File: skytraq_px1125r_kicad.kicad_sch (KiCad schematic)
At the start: 11 parts, among them J1 Conn_01x04, J2 SMA, J3 SH_Conn_01x04, J4 Conn_01x04, U1 Skytraq_PX1125R

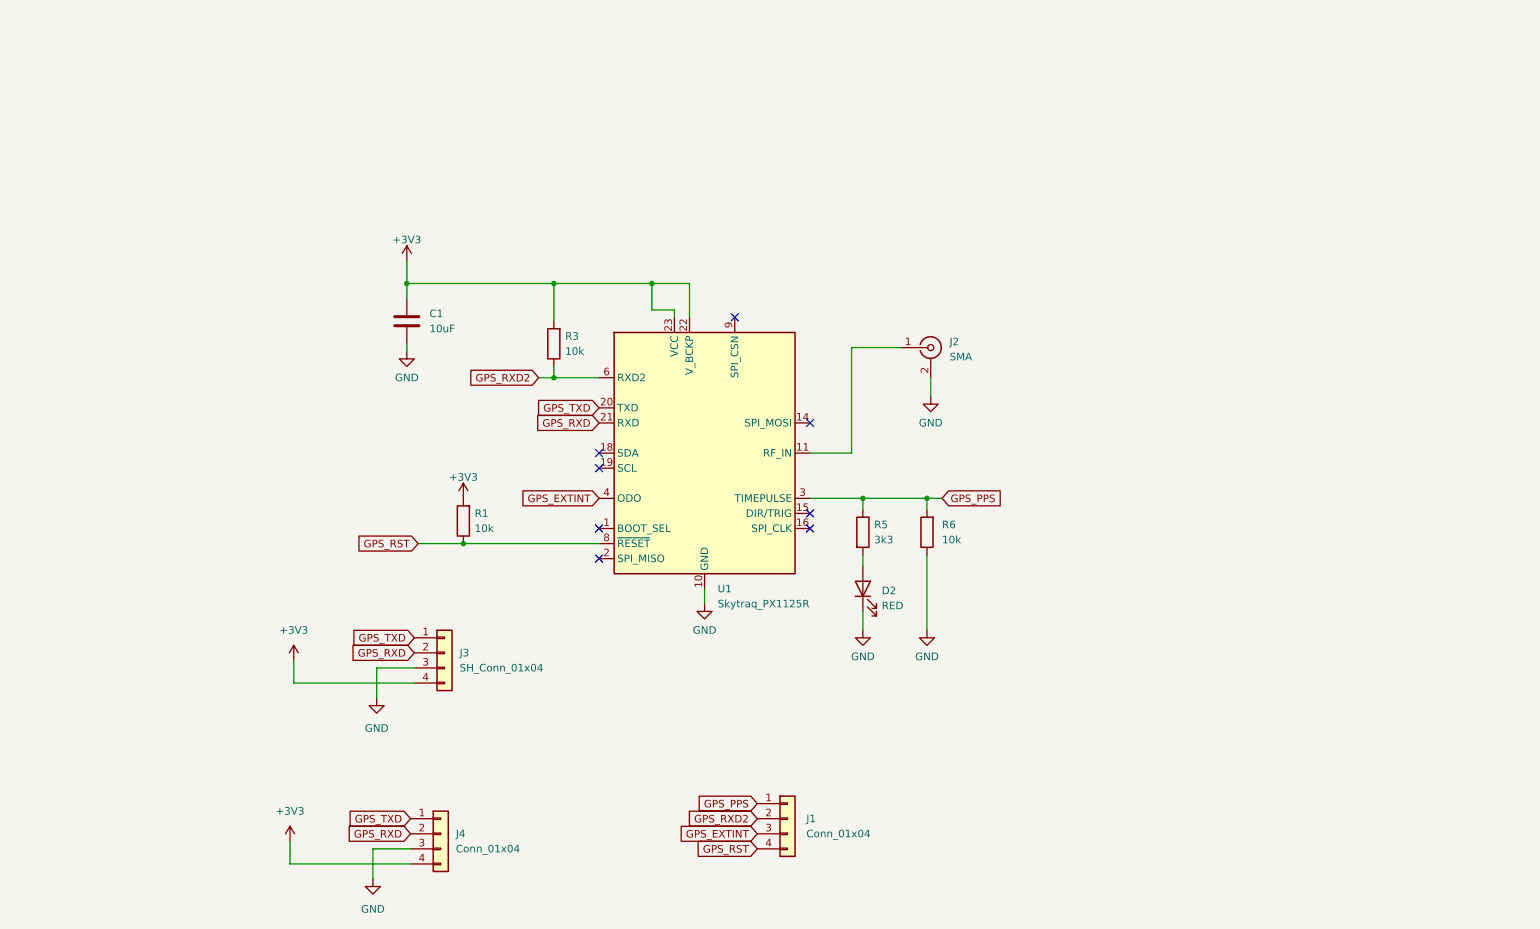
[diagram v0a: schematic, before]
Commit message: 36x36 flight controller board
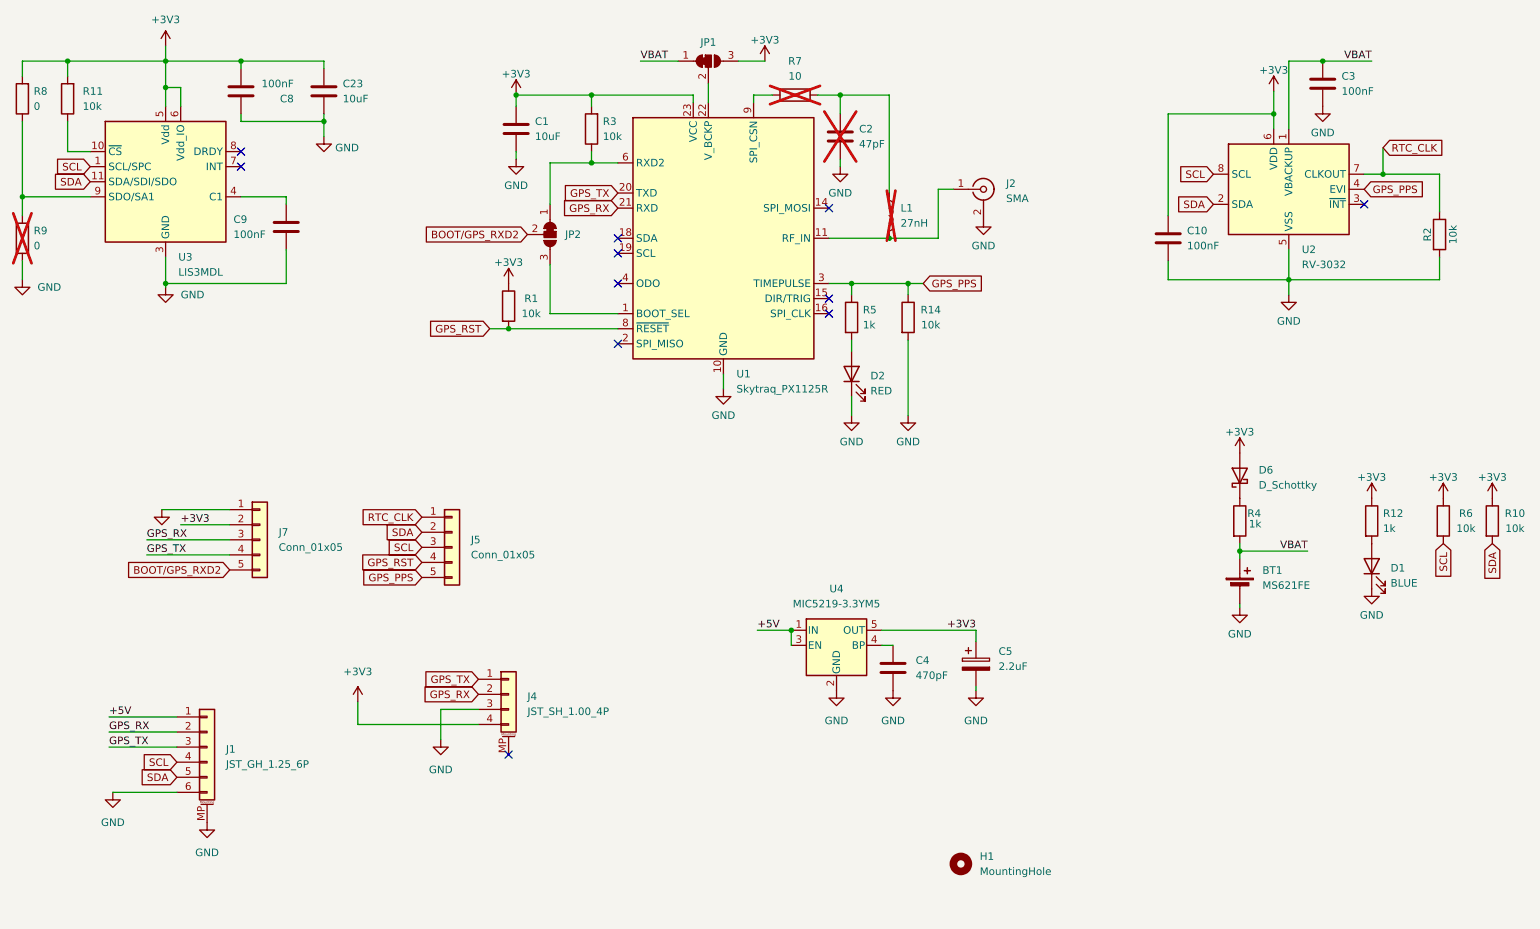
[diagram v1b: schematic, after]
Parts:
- removed J1, J4: Conn_01x04, Connector_PinHeader_2.54mm:PinHeader_1x04_P2.54mm_Vertical, symbol Connector_Generic:Conn_01x04
- removed J3: SH_Conn_01x04, Connector_JST:JST_SH_SM04B-SRSS-TB_1x04-1MP_P1.00mm_Horizontal, symbol Connector_Generic:Conn_01x04
- added BT1: MS621FE, Battery:BatteryHolder_Seiko_MS621F, symbol Device:Battery_Cell
- added C10, C3, C8, C9: 100nF, Capacitor_SMD:C_0402_1005Metric, symbol Device:C
- added C2: 47pF, Capacitor_SMD:C_0603_1608Metric, symbol Device:C
- added C23: 10uF, Capacitor_SMD:C_0603_1608Metric, symbol Device:C
- added C4: 470pF, Capacitor_SMD:C_0603_1608Metric_Pad1.08x0.95mm_HandSolder, symbol Device:C
- added C5: 2.2uF, Capacitor_Tantalum_SMD:CP_EIA-3216-18_Kemet-A, symbol Device:C_Polarized
- added D1: BLUE, LED_SMD:LED_0603_1608Metric, symbol Device:LED
- added D6: D_Schottky, Diode_SMD:D_SMB, symbol Device:D_Schottky
- added H1: MountingHole, MountingHole:MountingHole_3.2mm_M3, symbol Mechanical:MountingHole
- added J1: JST_GH_1.25_6P, Connector_JST:JST_GH_SM06B-GHS-TB_1x06-1MP_P1.25mm_Horizontal, symbol Connector_Generic_MountingPin:Conn_01x06_MountingPin
- added J4: JST_SH_1.00_4P, Connector_JST:JST_SH_SM04B-SRSS-TB_1x04-1MP_P1.00mm_Horizontal, symbol Connector_Generic_MountingPin:Conn_01x04_MountingPin
- added J5, J7: Conn_01x05, Connector_PinHeader_2.54mm:PinHeader_1x05_P2.54mm_Horizontal, symbol Connector_Generic:Conn_01x05
- added JP1, JP2: SolderJumper_3_Bridged12, Jumper:SolderJumper-3_P1.3mm_Bridged12_RoundedPad1.0x1.5mm, symbol Jumper:SolderJumper_3_Bridged12
- added L1: 27nH, Inductor_SMD:L_0603_1608Metric, symbol Device:L
- added R10, R11, R14, R2: 10k, Resistor_SMD:R_0603_1608Metric, symbol Device:R
- added R12, R4: 1k, Resistor_SMD:R_0603_1608Metric, symbol Device:R
- added R7: 10, Resistor_SMD:R_0603_1608Metric, symbol Device:R
- added R8, R9: 0, Resistor_SMD:R_0603_1608Metric, symbol Device:R
- added U2: RV-3032, MyFootprints:RV-3032, symbol MySymbols:RV-3032
- added U3: LIS3MDL, footprint_JLCPCB:LGA-12_L2.0-W2.0-P0.50-BL, symbol Sensor_Magnetic:LIS3MDL
- added U4: MIC5219-3.3YM5, Package_TO_SOT_SMD:SOT-23-5, symbol Regulator_Linear:MIC5219-3.3YM5
- C1: footprint Capacitor_SMD:C_0805_2012Metric_Pad1.18x1.45mm_HandSolder -> Capacitor_SMD:C_0603_1608Metric; Note (none) -> Low ESR! X7R; OriginalVal 4u7/10V -> (none)
- D2: footprint LED_SMD:LED_0805_2012Metric_Pad1.15x1.40mm_HandSolder -> LED_SMD:LED_0603_1608Metric; LCSC (none) -> C2286; Note (none) -> PPS
- J2: footprint Connector_Coaxial:SMA_Amphenol_901-143_Horizontal -> footprint_JLCPCB:SMA-SMD_BWSMA-KE-P001; LCSC (none) -> C496550
- R1, R3, R6: footprint Resistor_SMD:R_0805_2012Metric_Pad1.20x1.40mm_HandSolder -> Resistor_SMD:R_0603_1608Metric; LCSC (none) -> C25804
- R5: value 3k3 -> 1k; footprint Resistor_SMD:R_0805_2012Metric_Pad1.20x1.40mm_HandSolder -> Resistor_SMD:R_0603_1608Metric; LCSC (none) -> C21190; OriginalVal 4k7 -> (none)
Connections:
- net +3V3: now also C1.1, R1.1, R6.1, C10.1, C23.2, C5.1, C8.1, D6.2 (A), J4.4 (Pin_4), J7.2 (Pin_2), JP1.3 (B), R10.1, R11.2, R12.1, R8.2, U2.6 (VDD), U3.5 (Vdd), U3.6 (Vdd_IO), U4.5 (OUT); no longer C1.2, R1.2, U1.22 (V_BCKP)
- net GND: now also C1.2, BT1.2 (-), C10.2, C2.2, C23.1, C3.2, C4.2, C5.2, C8.2, C9.1, D1.1 (K), J1.6 (Pin_6), J1.MP (MountPin), J4.3 (Pin_3), J7.1 (Pin_1), R14.2, R2.2, R9.1, U2.5 (VSS), U3.12 (GND), U3.2 (GND), U3.3 (GND), U4.2 (GND); no longer C1.1, R6.1
- net GPS_PPS: now also J5.5 (Pin_5), R14.1, U2.4 (EVI); no longer R6.2
- net GPS_RST: now also R1.2, J5.4 (Pin_4); no longer R1.1
- net at J2.1 (In), U1.11 (RF_IN): now also L1.2
- net at U1.1 (BOOT_SEL): now also JP2.3 (B)
- net at U1.9 (SPI_CSN): now also R7.1
- net GPS_EXTINT: no longer names the net of U1.4 (ODO)
- net GPS_RXD renamed GPS_RX
- net GPS_RX: now also J1.2 (Pin_2), J4.2 (Pin_2), J7.3 (Pin_3)
- net GPS_RXD2: no longer names the net of R3.1, U1.6 (RXD2)
- net GPS_RXD2: now also JP2.1 (A)
- net GPS_TXD renamed GPS_TX
- net GPS_TX: now also J1.3 (Pin_3), J4.1 (Pin_1), J7.4 (Pin_4)
- new net: C2.1, L1.1, R7.2
- new net: R8.1, R9.2, U3.9 (SDO/SA1)
- new net: C4.1, U4.4 (BP)
- new net: D1.2 (A), R12.2
- new net: JP1.2 (C), U1.22 (V_BCKP)
- new net: C9.2, U3.4 (C1)
- new net: D6.1 (K), R4.1
- new net: R11.1, U3.10 (~{CS})
- new net +5V: J1.1 (Pin_1), U4.1 (IN), U4.3 (EN)
- new net BOOT/GPS_RXD2: J7.5 (Pin_5), JP2.2 (C)
- new net RTC_CLK: J5.1 (Pin_1), R2.1, U2.7 (CLKOUT)
- new net SCL: J1.4 (Pin_4), J5.3 (Pin_3), R6.2, U2.8 (SCL), U3.1 (SCL/SPC)
- new net SDA: J1.5 (Pin_5), J5.2 (Pin_2), R10.2, U2.2 (SDA), U3.11 (SDA/SDI/SDO)
- new net VBAT: BT1.1 (+), C3.1, JP1.1 (A), R4.2, U2.1 (VBACKUP)
- no-connect marks 8 -> 11
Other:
- moved on the sheet: J2, R3, U1

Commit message: with px1105 unfinished
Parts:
- removed C4: 470pF, Capacitor_SMD:C_0603_1608Metric_Pad1.08x0.95mm_HandSolder, symbol Device:C
- removed C5: 2.2uF, Capacitor_Tantalum_SMD:CP_EIA-3216-18_Kemet-A, symbol Device:C_Polarized
- removed J4: JST_SH_1.00_4P, Connector_JST:JST_SH_SM04B-SRSS-TB_1x04-1MP_P1.00mm_Horizontal, symbol Connector_Generic_MountingPin:Conn_01x04_MountingPin
- removed J5, J7: Conn_01x05, Connector_PinHeader_2.54mm:PinHeader_1x05_P2.54mm_Horizontal, symbol Connector_Generic:Conn_01x05
- removed U4: MIC5219-3.3YM5, Package_TO_SOT_SMD:SOT-23-5, symbol Regulator_Linear:MIC5219-3.3YM5
- added C6: 22uF, Capacitor_Tantalum_SMD:CP_EIA-3216-18_Kemet-A, symbol Device:C_Polarized
- added C7: 10uF, Capacitor_SMD:C_0603_1608Metric, symbol Device:C
- added J5: Conn_01x04, Connector_PinSocket_2.54mm:PinSocket_1x04_P2.54mm_Vertical, symbol Connector_Generic:Conn_01x04
- added J7: Conn_01x06, Connector_PinHeader_2.54mm:PinHeader_1x06_P2.54mm_Vertical, symbol Connector_Generic:Conn_01x06
- added U5: ~, MyFootprints:skytraq_px1105, symbol MySkyTraqSymbols:SkyTraq_PX1105
- added U6: AMS1117-3.3, Package_TO_SOT_SMD:SOT-223-3_TabPin2, symbol Regulator_Linear:AMS1117-3.3
- D6: footprint Diode_SMD:D_SMB -> Diode_SMD:D_SOD-323
- J2: footprint footprint_JLCPCB:SMA-SMD_BWSMA-KE-P001 -> footprint_JLCPCB:SMA-SMD_BWSMA-KE-P001_Symmetric
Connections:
- net +3V3: now also C6.1, J7.2 (Pin_2), U5.8 (VCC), U6.2 (VO)
- net +5V: now also C7.2, U6.3 (VI)
- net BOOT/GPS_RXD2: now also J7.6 (Pin_6)
- net GND: now also C6.2, C7.1, J7.1 (Pin_1), U5.1 (GND), U6.1 (GND)
- net GPS_PPS: now also J7.5 (Pin_5), U5.4 (PPS)
- net GPS_RST: now also J5.4 (Pin_4), U5.9 (~{RESET})
- net GPS_RX: now also J7.3 (Pin_3), U5.3 (RXD)
- net GPS_TX: now also J7.4 (Pin_4), U5.2 (TXD)
- net RTC_CLK: now also J5.1 (Pin_1)
- net SCL: now also J5.3 (Pin_3)
- net SDA: now also J5.2 (Pin_2)
- net GPS_RF: now reaches J2.1 (In), L1.2, U1.11 (RF_IN)
- net GPS_RF: now also U5.11 (RF_IN)
- net GPS_V_BCKP: now reaches JP1.2 (C), U1.22 (V_BCKP)
- net GPS_V_BCKP: now also U5.6 (V_BCKP)
- net GPS_RX2: now reaches JP2.1 (A), R3.1, U1.6 (RXD2)
- net GPS_RX2: now also U5.15 (RXD2)
- net GPS_BOOT: now reaches JP2.3 (B), U1.1 (BOOT_SEL)
- net GPS_BOOT: now also U5.18 (BOOT_SEL)
- no-connect marks 11 -> 14
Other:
- moved on the sheet: BT1, C1, D1, D6, J1, JP1, JP2, R1, R10, R12, R3, R4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

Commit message: px1105 4-layers boar
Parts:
- removed J5: Conn_01x04, Connector_PinSocket_2.54mm:PinSocket_1x04_P2.54mm_Vertical, symbol Connector_Generic:Conn_01x04
- added C4: 100nF, Capacitor_SMD:C_0402_1005Metric, symbol Device:C
- added C5: 10uF, Capacitor_SMD:C_0603_1608Metric, symbol Device:C
- added J3: JST_GH_1.25_6P, Connector_JST:JST_GH_SM06B-GHS-TB_1x06-1MP_P1.25mm_Horizontal, symbol Connector_Generic_MountingPin:Conn_01x06_MountingPin
- added J5: Conn_01x06, Connector_PinHeader_2.54mm:PinHeader_1x06_P2.54mm_Vertical, symbol Connector_Generic:Conn_01x06
- U6: footprint Package_TO_SOT_SMD:SOT-223-3_TabPin2 -> Package_TO_SOT_SMD:SOT-89-3
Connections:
- net +3V3: now also J7.1 (Pin_1), C5.1; no longer J7.2 (Pin_2)
- net +5V: now also J3.1 (Pin_1), J5.1 (Pin_1)
- net BOOT/GPS_RXD2: now also J3.2 (Pin_2)
- net GND: now also J7.2 (Pin_2), C4.2, C5.2, J3.6 (Pin_6), J5.2 (Pin_2); no longer J1.MP (MountPin), J7.1 (Pin_1)
- net GPS_PPS: now also J3.3 (Pin_3)
- net GPS_RST: now also J3.5 (Pin_5), J5.6 (Pin_6)
- net GPS_V_BCKP: now also C4.1
- net RTC_CLK: now also J3.4 (Pin_4), J5.3 (Pin_3)
- net SCL: now also J5.5 (Pin_5)
- net SDA: now also J5.4 (Pin_4)
- no-connect marks 14 -> 16
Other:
- moved on the sheet: U5

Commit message: added 2 M3 mounting holes
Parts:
- added D3: GREEN, LED_SMD:LED_0603_1608Metric, symbol Device:LED
- added H2, H3, H4: MountingHole, MountingHole:MountingHole_3.2mm_M3, symbol Mechanical:MountingHole
- added R13: 1k, Resistor_SMD:R_0603_1608Metric, symbol Device:R
- C4: footprint Capacitor_SMD:C_0402_1005Metric -> Capacitor_SMD:C_0805_2012Metric_Pad1.18x1.45mm_HandSolder; LCSC C1525 -> (none); Note Low ESR! X7R -> (none); now left out of the parts list
- C5: footprint Capacitor_SMD:C_0603_1608Metric -> Capacitor_SMD:C_0805_2012Metric_Pad1.18x1.45mm_HandSolder; LCSC C19702 -> (none); Note Low ESR! X7R -> (none); now left out of the parts list
- J2: footprint footprint_JLCPCB:SMA-SMD_BWSMA-KE-P001_Symmetric -> footprint:SMA-SMD_BWSMA-KE-P001_Symmetric
- U3: footprint footprint_JLCPCB:LGA-12_L2.0-W2.0-P0.50-BL -> footprint:LGA-12_L2.0-W2.0-P0.50-BL
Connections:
- net +3V3: now also R13.1
- net GPS_RX2: now also D3.1 (K)
- net BOOT/GPS_RXD2 renamed BOOT/GPS_RX2
- new net: D3.2 (A), R13.2

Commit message: one more M3 hole
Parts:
- C3: value 100nF -> 10uF; footprint Capacitor_SMD:C_0402_1005Metric -> Capacitor_SMD:C_0603_1608Metric; LCSC C1525 -> C19702
- U5: value ~ -> SkyTraq_PX1105; now left out of the parts list
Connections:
- net GPS_V_BCKP: now also C3.1
- net VBAT: no longer C3.1
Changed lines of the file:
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@@
 	)
 	(junction
-		(at 241.935 26.67)
-		(diameter 0)
-		(color 0 0 0 0)
-	)
-	(junction
 		(at 252.095 45.72)
 		(diameter 0)
@@
 	(wire
 		(pts
+			(xy 138.557 27.178) (xy 138.557 27.305)
+		)
+		(stroke
+			(width 0)
+			(type default)
+		)
+	)
+	(wire
+		(pts
 			(xy 111.125 43.815) (xy 123.19 43.815)
 		)
@@
 	(wire
 		(pts
-			(xy 236.22 26.67) (xy 236.22 38.1)
+			(xy 236.22 35.306) (xy 236.22 38.1)
 		)
 		(stroke
@@
 	(wire
 		(pts
+			(xy 138.557 27.305) (xy 138.43 27.305)
+		)
+		(stroke
+			(width 0)
+			(type default)
+		)
+	)
+	(wire
+		(pts
 			(xy 30.48 36.83) (xy 30.48 41.91)
 		)
@@
 	(wire
 		(pts
-			(xy 236.22 26.67) (xy 241.935 26.67)
+			(xy 236.22 35.306) (xy 240.284 35.306)
 		)
 		(stroke
@@
 	(wire
 		(pts
-			(xy 241.935 26.67) (xy 250.19 26.67)
-		)
-		(stroke
-			(width 0)
-			(type default)
-		)
-	)
-	(wire
-		(pts
 			(xy 67.31 64.135) (xy 46.99 64.135)
 		)
@@
 	(wire
 		(pts
-			(xy 150.495 27.305) (xy 138.43 27.305)
+			(xy 150.622 27.178) (xy 138.557 27.178)
 		)
 		(stroke
@@
 	)
 	(label "VBAT"
-		(at 250.19 26.67 180)
+		(at 240.284 35.306 180)
 		(effects
 			(font
@@
 	)
 	(label "GPS_V_BCKP"
-		(at 150.495 27.305 180)
+		(at 150.622 27.178 180)
 		(effects
 			(font
@@
 		(on_board yes)
 		(dnp yes)
-		(fields_autoplaced yes)
 		(property "Reference" "R7"
-			(at 153.035 26.67 90)
+			(at 147.828 31.242 90)
 			(effects
 				(font
@@
 		)
 		(property "Value" "10"
-			(at 153.035 29.21 90)
+			(at 152.908 32.512 90)
 			(effects
 				(font
@@
 	(symbol
 		(lib_id "power:GND")
-		(at 241.935 34.29 0)
-		(unit 1)
-		(exclude_from_sim no)
-		(in_bom yes)
-		(on_board yes)
-		(dnp no)
-		(fields_autoplaced yes)
-		(property "Reference" "#PWR04"
-			(at 241.935 40.64 0)
-			(effects
-				(font
-					(size 1.27 1.27)
-				)
-				(hide yes)
-			)
-		)
-		(property "Value" "GND"
-			(at 241.935 38.735 0)
-			(effects
-				(font
-					(size 1.27 1.27)
-				)
-			)
-		)
-		(property "Footprint" ""
-			(at 241.935 34.29 0)
-			(effects
-				(font
-					(size 1.27 1.27)
-				)
-				(hide yes)
-			)
-		)
-		(property "Datasheet" "~"
-			(at 241.935 34.29 0)
-			(effects
-				(font
-					(size 1.27 1.27)
-				)
-				(hide yes)
-			)
-		)
-		(property "Description" "Power symbol creates a global label with name \"GND\" , ground"
-			(at 241.935 34.29 0)
-			(effects
-				(font
-					(size 1.27 1.27)
-				)
-				(hide yes)
-			)
-		)
-		(pin "1"
-		)
-		(instances
-			(project "skytraq_px1125r_kicad"
-				(path "/f8f1d4cf-0f7a-4055-9a9d-a328f34ee721"
-					(reference "#PWR04")
-					(unit 1)
-				)
-			)
-		)
-	)
-	(symbol
-		(lib_id "power:GND")
 		(at 123.825 109.22 0)
 		(unit 1)
@@
 		(unit 1)
 		(exclude_from_sim no)
-		(in_bom yes)
+		(in_bom no)
 		(on_board yes)
 		(dnp no)
@@
 			)
 		)
-		(property "Value" "~"
+		(property "Value" "SkyTraq_PX1105"
 			(at 138.6683 142.24 0)
 			(effects
@@
 	)
 	(symbol
+		(lib_id "power:GND")
+		(at 158.242 27.178 0)
+		(unit 1)
+		(exclude_from_sim no)
+		(in_bom yes)
+		(on_board yes)
+		(dnp no)
+		(fields_autoplaced yes)
+		(property "Reference" "#PWR04"
+			(at 158.242 33.528 0)
+			(effects
+				(font
+					(size 1.27 1.27)
+				)
+				(hide yes)
+			)
+		)
+		(property "Value" "GND"
+			(at 158.242 31.623 0)
+			(effects
+				(font
+					(size 1.27 1.27)
+				)
+			)
+		)
+		(property "Footprint" ""
+			(at 158.242 27.178 0)
+			(effects
+				(font
+					(size 1.27 1.27)
+				)
+				(hide yes)
+			)
+		)
+		(property "Datasheet" ""
+			(at 158.242 27.178 0)
+			(effects
+				(font
+					(size 1.27 1.27)
+				)
+				(hide yes)
+			)
+		)
+		(property "Description" ""
+			(at 158.242 27.178 0)
+			(effects
+				(font
+					(size 1.27 1.27)
+				)
+			)
+		)
+		(pin "1"
+		)
+		(instances
+			(project "skytraq_px1125r_kicad"
+				(path "/f8f1d4cf-0f7a-4055-9a9d-a328f34ee721"
+					(reference "#PWR04")
+					(unit 1)
+				)
+			)
+		)
+	)
+	(symbol
 		(lib_id "Device:C")
 		(at 98.425 38.1 0)
@@
 	)
 	(symbol
-		(lib_id "Device:C")
-		(at 241.935 30.48 0)
-		(unit 1)
-		(exclude_from_sim no)
-		(in_bom yes)
-		(on_board yes)
-		(dnp no)
-		(property "Reference" "C3"
-			(at 245.11 29.21 0)
-			(effects
-				(font
-					(size 1.27 1.27)
-				)
-				(justify left)
-			)
-		)
-		(property "Value" "100nF"
-			(at 245.11 31.75 0)
-			(effects
-				(font
-					(size 1.27 1.27)
-				)
-				(justify left)
-			)
-		)
-		(property "Footprint" "Capacitor_SMD:C_0402_1005Metric"
-			(at 242.9002 34.29 0)
-			(effects
-				(font
-					(size 1.27 1.27)
-				)
-				(hide yes)
-			)
-		)
-		(property "Datasheet" "~"
-			(at 241.935 30.48 0)
-			(effects
-				(font
-					(size 1.27 1.27)
-				)
-				(hide yes)
-			)
-		)
-		(property "Description" "Unpolarized capacitor"
-			(at 241.935 30.48 0)
-			(effects
-				(font
-					(size 1.27 1.27)
-				)
-				(hide yes)
-			)
-		)
-		(property "LCSC" "C1525"
-			(at 241.935 30.48 0)
-			(effects
-				(font
-					(size 1.27 1.27)
-				)
-				(hide yes)
-			)
-		)
-		(property "Note" "Low ESR! X7R"
-			(at 241.935 30.48 0)
-			(effects
-				(font
-					(size 1.27 1.27)
-				)
-				(hide yes)
-			)
-		)
-		(pin "1"
-		)
-		(pin "2"
-		)
-		(instances
-			(project "skytraq_px1125r_kicad"
-				(path "/f8f1d4cf-0f7a-4055-9a9d-a328f34ee721"
-					(reference "C3")
-					(unit 1)
-				)
-			)
-		)
-	)
-	(symbol
 		(lib_id "Device:R")
 		(at 172.085 69.85 0)
@@
 					(unit 1)
 				)
+			)
+		)
+	)
+	(symbol
+		(lib_id "Device:C")
+		(at 154.432 27.178 90)
+		(unit 1)
+		(exclude_from_sim no)
+		(in_bom yes)
+		(on_board yes)
+		(dnp no)
+		(property "Reference" "C3"
+			(at 153.162 24.003 0)
+			(effects
+				(font
+					(size 1.27 1.27)
+				)
+				(justify left)
+			)
+		)
+		(property "Value" "10uF"
+			(at 155.702 24.003 0)
+			(effects
+				(font
+					(size 1.27 1.27)
+				)
+				(justify left)
+			)
+		)
+		(property "Footprint" "Capacitor_SMD:C_0603_1608Metric"
+			(at 158.242 26.2128 0)
+			(effects
+				(font
+					(size 1.27 1.27)
+				)
+				(hide yes)
+			)
+		)
+		(property "Datasheet" "~"
+			(at 154.432 27.178 0)
+			(effects
+				(font
+					(size 1.27 1.27)
+				)
+				(hide yes)
+			)
+		)
+		(property "Description" "Unpolarized capacitor"
+			(at 154.432 27.178 0)
+			(effects
+				(font
+					(size 1.27 1.27)
+				)
+				(hide yes)
+			)
+		)
+		(property "LCSC" "C19702"
+			(at 154.432 27.178 0)
+			(effects
+				(font
+					(size 1.27 1.27)
+				)
+				(hide yes)
+			)
+		)
+		(property "Note" "Low ESR! X7R"
+			(at 154.432 27.178 0)
+			(effects
+				(font
+					(size 1.27 1.27)
+				)
+				(hide yes)
+			)
+		)
+		(pin "1"
+		)
+		(pin "2"
+		)
+		(instances
+			(project "skytraq_px1125r_kicad"
+				(path "/f8f1d4cf-0f7a-4055-9a9d-a328f34ee721"
+					(reference "C3")
+					(unit 1)
+				)
